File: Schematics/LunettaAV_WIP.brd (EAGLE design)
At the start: 52 parts, among them IC1 TLC339P, IC2 7805T, IC3 4046N, IC4 4040N, IC5 4017N, IC6 4051N, IC7 4094N, IC8 4046N, IC9 40106N, U1 LM358

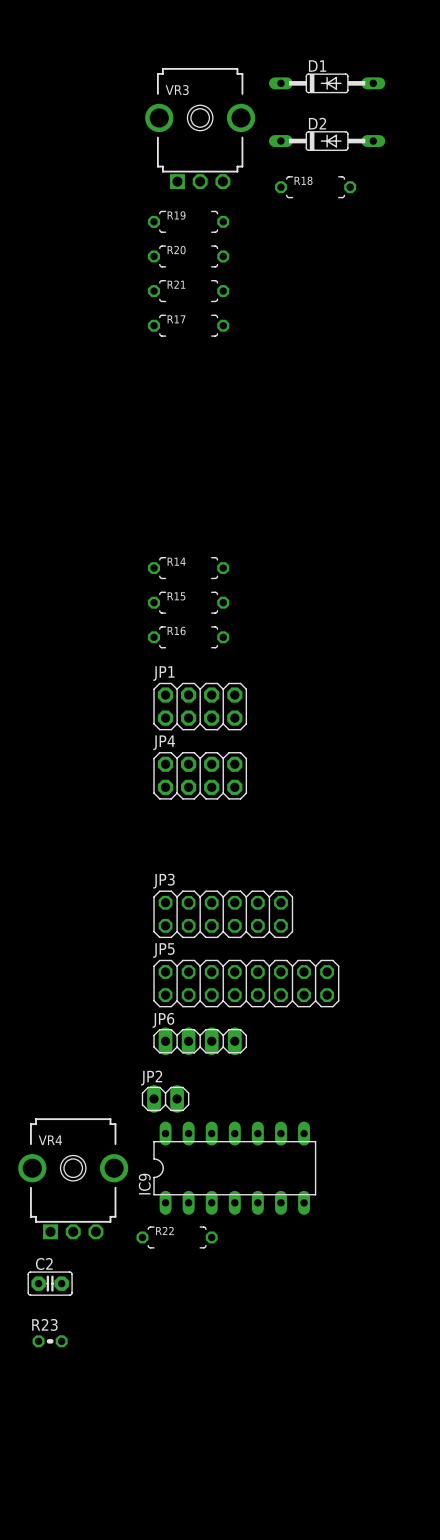
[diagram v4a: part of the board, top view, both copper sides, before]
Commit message: change melody out config and buffer the out for later stage
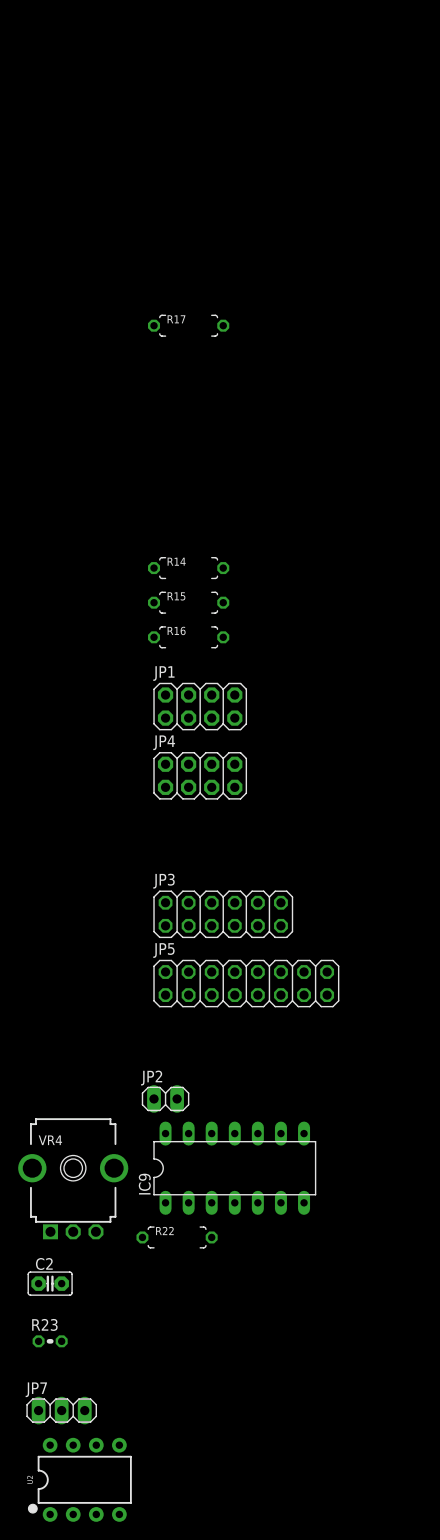
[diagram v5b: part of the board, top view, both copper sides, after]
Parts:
- removed D1, D2: 1N4148, diode:DO35-10
- removed JP6: (no value), pinhead:1X04
- removed R18, R19, R20: 100K, MusicThingModular:7MM_RESISTOR
- removed R21: 10K, MusicThingModular:7MM_RESISTOR
- removed VR3: 100K, MusicThingModular:9MM_SNAP-IN_POT
- added JP7: (no value), pinhead:1X03
- added U2: LM358, SparkFun-IC-Amplifiers:DIP08
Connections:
- removed net DRONEOUT: R20.1, VR3.2
- removed net GATEIN: JP6.4, R18.1
- removed net MIX: R19.2, R20.2, R21.2
- removed net N$7: D1.A, D2.A, R18.2
- removed net VCAOUT: D2.C, R19.1
- new net BUFFMEL: U2.6, U2.7
- net 9V: now also U2.8
- net GND: now also U2.4; no longer R21.1, VR3.1
- net MELODYOUT: now also U2.5; no longer D1.C, VR3.3
- net MOOX: now also JP7.3; no longer JP6.1
- net MOXO: now also JP7.2; no longer JP6.2
- net MXOO: now also JP7.1; no longer JP6.3

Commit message: PT2399 init + screen changed
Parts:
- removed DISP$1, DISP$2: DISPLAY-OLED-128X64-I2C, diy-modules:DISPLAY-OLED-128X64-I2C
- added C10, C8, C9: 10uF, SparkFun-Capacitors:CPOL-RADIAL-2.5MM-5MM
- added C11: 47uF, SparkFun-Capacitors:CPOL-RADIAL-2.5MM-5MM
- added C12, C13, C4, C5, C6, C7: 0.1uF, SparkFun-Capacitors:CAP-PTH-SMALL-KIT
- added C3: 100uF, SparkFun-Capacitors:CPOL-RADIAL-2.5MM-6.5MM
- added DD1: PT2399, ic-princeton-technologies:DIP-16
- added IC10: (no value), v-reg:78XXS
- added J1: POWER_JACKPOWER_JACK_SLOT, SparkFun-Connectors:POWER_JACK_PTH_SLOT
- added R13: (no value), MusicThingModular:7MM_RESISTOR
- added R18: 10k, MusicThingModular:7MM_RESISTOR
- added R19: 100k, MusicThingModular:7MM_RESISTOR
- added U$1, U$2: OLED_0.96_I2C, tft_1_8_1_44_oled_0_96:OLED_0.96_I2C
- added VR3: (no value), MusicThingModular:9MM_SNAP-IN_POT
- C1: value 1uF -> 10nF
- IC2: value 7805T -> 7805; device linear:TO220H -> v-reg:78XXS
- moved IC2 270.2 mm to (-138.4, -189.2)
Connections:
- new net DCIN: C10.1, IC10.IN, J1.PWR
- new net N$12: C6.1, DD1.10
- new net N$13: C7.2, DD1.11
- new net N$14: C7.1, DD1.12
- new net N$15: DD1.6, R13.2
- new net N$16: C11.1, DD1.2
- new net N$17: C5.2, DD1.7
- new net N$18: C4.1, DD1.8
- new net N$29: DD1.16, R18.1, R19.2
- new net N$30: DD1.15, R18.2
- new net N$7: C6.2, DD1.9
- net 3V3: now also C12.1, C13.1, U$1.VCC, U$2.VCC; no longer DISP$1.2, DISP$2.2
- net 5V: now also C3.1, C9.1, DD1.1, IC2.OUT; no longer IC2.3
- net 9V: now also C8.1, IC10.OUT, IC2.IN; no longer IC2.1
- net BUFFMEL: now also R19.1
- net GND: now also C10.2, C11.2, C12.2, C13.2, C3.2, C4.2, C5.1, C8.2, C9.2, DD1.3, DD1.4, IC10.GND, IC2.GND, J1.GND, U$1.GND, U$2.GND; no longer DISP$1.1, DISP$2.1, IC2.2
- net N$3: now also U$1.SCL, U$2.SCL; no longer DISP$1.3, DISP$2.3
- net N$4: now also U$1.SDA, U$2.SDA; no longer DISP$1.4, DISP$2.4
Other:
- board outline added: 7 x 7 mm

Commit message: PT Delay and other fixes
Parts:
- removed JP7: (no value), pinhead:1X03
- removed U$1, U$2: OLED_0.96_I2C, tft_1_8_1_44_oled_0_96:OLED_0.96_I2C
- added C14: .1uF, capacitor-wima:C2.5-2
- added C15, C16, C17, C19, C20, C21, C22: 0.1uF, SparkFun-Capacitors:CAP-PTH-SMALL-KIT
- added C18: 47uF, SparkFun-Capacitors:CPOL-RADIAL-2.5MM-5MM
- added C23: 100uF, SparkFun-Capacitors:CPOL-RADIAL-2.5MM-6.5MM
- added CLOCK-OUT, J3: WQP-PJ301M-12_JACK, MusicThingModular:WQP-PJ301M-12_JACK
- added D1: BAT42, diode:DO35-10
- added J2: (no value), SparkFun-Connectors:1X04_LONGPADS
- added OL96$1, OL96$2: OLED_0.96_I2C, tft_1_8_1_44_oled_0_96:OLED_0.96_I2C
- added R20: 10K, MusicThingModular:7MM_RESISTOR
- added R21: (no value), MusicThingModular:7MM_RESISTOR
- added VR5: (no value), MusicThingModular:9MM_SNAP-IN_POT
- C1: value 10nF -> 0.1uF; device SparkFun-Capacitors:CAP-PTH-10MM -> SparkFun-Capacitors:CAP-PTH-SMALL-KIT
- C10: value 10uF -> 10nF; device SparkFun-Capacitors:CPOL-RADIAL-2.5MM-5MM -> SparkFun-Capacitors:CAP-PTH-10MM
- C11: value 47uF -> 0.1uF; device SparkFun-Capacitors:CPOL-RADIAL-2.5MM-5MM -> SparkFun-Capacitors:CAP-PTH-SMALL-KIT
- C2: value .1uF -> 10uF; device capacitor-wima:C2.5-2 -> SparkFun-Capacitors:CPOL-RADIAL-2.5MM-5MM
- C3: value 100uF -> 10uF; device SparkFun-Capacitors:CPOL-RADIAL-2.5MM-6.5MM -> SparkFun-Capacitors:CPOL-RADIAL-2.5MM-5MM
- C5: value 0.1uF -> 10uF; device SparkFun-Capacitors:CAP-PTH-SMALL-KIT -> SparkFun-Capacitors:CPOL-RADIAL-2.5MM-5MM
- C8, C9: value 10uF -> 0.1uF; device SparkFun-Capacitors:CPOL-RADIAL-2.5MM-5MM -> SparkFun-Capacitors:CAP-PTH-SMALL-KIT
- IC1: value TLC339P -> 7809\; device linear:DIL14 -> v-reg:78XXS
- IC10: value (none) -> 4051N; device v-reg:78XXS -> 40xx:DIL16
- IC3: value 4046N -> 4040N
- IC4: value 4040N -> TLC339P; device 40xx:DIL16 -> linear:DIL14
- IC5: value 4017N -> 4046N
- IC6: value 4051N -> 4094N
- IC7: value 4094N -> 40106N; device 40xx:DIL16 -> 40xx:DIL14
- IC9: value 40106N -> 4017N; device 40xx:DIL14 -> 40xx:DIL16
- JP1: device adafruit:2X04 -> pinhead:1X02
- JP2: device pinhead:1X02 -> adafruit:2X04
- JP4: device adafruit:2X04 -> pinhead:2X08
- JP5: device pinhead:2X08 -> pinhead:1X03
- R1, R2: value 10K -> 4.7K; device MusicThingModular:7MM_RESISTOR -> MusicThingModular:10MM_RESISTOR
- R13: value (none) -> 1K
- R14: value 10K -> 1K
- R15: value 10K -> LDR; device MusicThingModular:7MM_RESISTOR -> rcl:0204V
- R16: value 10K -> 100k
- R17: value 1K -> 10k
- R18: value 10k -> 10K
- R19: value 100k -> 10K
- R22: value 1K -> (none)
- R23: value LDR -> (none); device rcl:0204V -> MusicThingModular:7MM_RESISTOR
- R3: value 10K -> 1K; device MusicThingModular:7MM_RESISTOR -> MusicThingModular:10MM_RESISTOR
- R5: value 1K -> 10K; device MusicThingModular:10MM_RESISTOR -> MusicThingModular:7MM_RESISTOR
- R6, R9: value 4.7K -> 10K; device MusicThingModular:10MM_RESISTOR -> MusicThingModular:7MM_RESISTOR
- S1, S2, S3: value (none) -> MOMENTARY-SWITCH-SPST-PTH-12MM
- VR3: value (none) -> 100K
- VR4: value 100K -> (none)
- moved R19 415.3 mm to (-78.7, 114.3)
- moved C13 415.0 mm to (-67.3, 118.1)
- moved R18 414.3 mm to (-68.6, 114.3)
- moved C12 413.3 mm to (-61.0, 118.1)
- moved C11 409.7 mm to (-54.6, 118.1)
- moved C3 370.4 mm to (-102.9, 94.0)
- moved R13 355.2 mm to (-27.9, 114.3)
- moved C8 334.9 mm to (-41.9, 118.1)
- moved C9 334.9 mm to (-48.3, 118.1)
- moved C10 325.2 mm to (-71.1, 102.9)
- moved C7 322.5 mm to (-35.6, 118.1)
- moved C6 321.1 mm to (-29.2, 118.1)
- moved C4 316.3 mm to (-22.9, 118.1)
- moved J1 312.2 mm to (-43.2, 83.8)
- moved C5 309.4 mm to (-16.5, 104.1)
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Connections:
- removed net VDD: IC9.14
- removed net VSS: IC9.7
- new net N$31: C19.2, DD1.11
- new net N$32: CLOCK-OUT.P$1_TIP, D1.C
- new net OUT: VR5.2
- net 3V3: now also C1.1, C4.1, OL96$1.VCC, OL96$2.VCC, R1.2, R2.2, R5.2; no longer C12.1, C13.1, R10.2, R11.2, R9.2, U$1.VCC, U$2.VCC
- net 5V: now also C23.1, C5.1, IC4.10, IC4.4, IC4.6, IC4.8, JP1.1; no longer C3.1, C9.1, IC1.10, IC1.4, IC1.6, IC1.8, JP2.1
- net 9V: now also C11.1, C12.1, C13.1, C15.1, C16.1, C17.1, C3.1, C6.1, C7.1, C9.1, IC1.OUT, IC10.16, IC4.3, IC6.1, IC6.15, IC7.14, IC9.16, R13.1; no longer IC1.3, IC10.OUT, IC4.16, IC7.1, IC7.15, IC7.16, R22.1
- net ANALOGIN1: no longer U1.3
- net ANALOGIN2: now also U1.3
- net AUDIORATE: now also IC7.6, IC9.14; no longer IC5.14, IC9.6
- net BUFFCLOCK: now also IC6.3, R22.1; no longer IC7.3
- net BUFFMEL: now also R16.1, VR5.3; no longer R19.1
- net CLOCKSELECT: now also JP2.2, JP2.4, JP2.6, JP2.8; no longer JP4.2, JP4.4, JP4.6, JP4.8
- net DCIN: now also C2.1, IC1.IN; no longer C10.1, IC10.IN
- net DIN1: now also R3.2; no longer R5.2
- net GND: now also C1.2, C14.2, C15.2, C16.2, C17.2, C18.2, C19.1, C20.1, C22.2, C23.2, C5.2, C6.2, C7.2, CLOCK-OUT.P$3_SLEEVE, DD1.12, IC1.GND, IC10.6, IC10.7, IC10.8, IC4.12, IC5.5, IC7.11, IC7.13, IC7.7, IC7.9, IC9.8, OL96$1.GND, OL96$2.GND, R10.1, R11.1, R18.1, R19.1, R20.1, R23.2, R9.1, VR4.1, VR5.1; no longer C10.2, C5.1, IC1.12, IC10.GND, IC3.5, IC4.8, IC5.13, IC6.6, IC6.7, IC7.8, IC9.11, IC9.9, R1.1, R14.1, R15.1, R16.1, R2.1, R5.1, U$1.GND, U$2.GND
- net MELODYOUT: now also IC9.3; no longer IC5.3
- net MOOX: now also IC10.9, JP5.3, R20.2; no longer IC6.9, JP7.3, R16.2
- net MOXO: now also IC10.10, JP5.2, R19.2; no longer IC6.10, JP7.2, R15.2
- net MXOO: now also IC10.11, JP5.1, R18.2; no longer IC6.11, JP7.1, R14.2
- net N$1: now also JP1.2; no longer JP2.2
- net N$10: now also IC7.4, IC7.5; no longer IC9.4, IC9.5
- net N$11: now also C14.1, IC7.1, R15.2, VR3.2; no longer C2.1, IC9.1, R23.2, VR4.2
- net N$12: now also C21.1; no longer C6.1
- net N$13: now also R22.2, R23.1, U2.3; no longer C7.2, DD1.11
- net N$14: now also D1.A, U2.1, U2.2; no longer C7.1, DD1.12
- net N$15: now also R21.2; no longer R13.2
- net N$16: now also C18.1; no longer C11.1
- net N$17: now also C20.2; no longer C5.2
- net N$18: now also C22.1; no longer C4.1
- net N$19: now also IC10.3, IC9.15; no longer IC5.15, IC6.3
- net N$2: now also C10.2, IC5.7; no longer C1.2, IC3.7
- net N$20: now also IC10.13, IC9.4; no longer IC5.4, IC6.13
- net N$21: now also IC10.14, IC9.7; no longer IC5.7, IC6.14
- net N$22: now also IC10.15, IC9.10; no longer IC5.10, IC6.15
- net N$23: now also IC10.12, IC9.1; no longer IC5.1, IC6.12
- net N$24: now also IC10.1, IC9.5; no longer IC5.5, IC6.1
- net N$25: now also IC10.5, IC9.6; no longer IC5.6, IC6.5
- net N$26: now also IC10.2, IC9.9; no longer IC5.9, IC6.2
- net N$27: now also IC10.4, IC9.11; no longer IC5.11, IC6.4
- net N$28: now also IC6.2, R14.1; no longer IC7.2, R17.1
- net N$29: now also R16.2, R17.1; no longer R18.1, R19.2
- net N$3: now also OL96$1.SCL, OL96$2.SCL, R1.1; no longer R6.1, U$1.SCL, U$2.SCL
- net N$30: now also R17.2, VR4.2; no longer R18.2
- net N$4: now also OL96$1.SDA, OL96$2.SDA, R2.1; no longer R9.1, U$1.SDA, U$2.SDA
- net N$5: now also C10.1, IC5.6; no longer C1.1, IC3.6
- net N$6: now also IC5.11; no longer IC3.11
- net N$7: now also C21.2; no longer C6.2
- net N$8: now also R13.2; no longer R22.2
- net N$9: now also IC7.2, IC7.3, R15.1, VR3.3; no longer IC9.2, IC9.3, R23.1, VR4.3
- net OOX: now also IC4.11, J2.4, R11.2; no longer IC1.11, JP1.1, JP1.2, R8.2
- net OXO: now also IC4.9, J2.3, R10.2; no longer IC1.9, JP1.3, JP1.4, R3.2
- net PLL/16: now also IC3.5; no longer IC4.5
- net PLL/2: now also IC3.9, JP2.3; no longer IC4.9, JP4.3
- net PLL/32: now also IC3.3; no longer IC4.3
- net PLL/4: now also IC3.7, JP2.5; no longer IC4.7, JP4.5
- net PLL/8: now also IC3.6, JP2.7; no longer IC4.6, JP4.7
- net PLLCLOCKOUT: now also IC3.10, IC5.4, JP2.1; no longer IC3.4, IC4.10, JP4.1
- net RESET: now also IC4.5, J2.1, R8.2; no longer IC1.5, JP1.7, JP1.8, R1.2
- net SPEEDYBUFF: now also IC5.9; no longer IC3.9
- net SR1: now also IC6.4, JP4.1, JP4.2; no longer IC7.4, JP5.1, JP5.2
- net SR2: now also IC6.5, JP4.3, JP4.4; no longer IC7.5, JP5.3, JP5.4
- net SR3: now also IC6.6, JP4.5, JP4.6; no longer IC7.6, JP5.5, JP5.6
- net SR4: now also IC6.7, JP4.7, JP4.8; no longer IC7.7, JP5.7, JP5.8
- net SR5: now also IC6.14, JP4.10, JP4.9; no longer IC7.14, JP5.10, JP5.9
- net SR6: now also IC6.13, JP4.11, JP4.12; no longer IC7.13, JP5.11, JP5.12
- net SR7: now also IC6.12, JP4.13, JP4.14; no longer IC7.12, JP5.13, JP5.14
- net SR8: now also IC6.11, JP4.15, JP4.16, R14.2; no longer IC7.11, JP5.15, JP5.16, R17.2
- net TNSYOOX: now also IC4.13, R7.1; no longer IC1.13, R11.1
- net TNSYOXO: now also IC4.14, R6.1; no longer IC1.14, R10.1
- net TNSYRES: now also IC4.2; no longer IC1.2
- net TNSYXOO: now also IC4.1, R5.1; no longer IC1.1, R7.1
- net XOO: now also IC4.7, J2.2, R9.2; no longer IC1.7, JP1.5, JP1.6, R2.2
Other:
- board size 7 x 7 mm -> 160 x 100 mm

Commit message: update schematics to match new code
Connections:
- net DIN1: now also B1.9; no longer B1.12
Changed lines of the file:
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@@
 </signal>
 <signal name="DIN1">
-<contactref element="B1" pad="12"/>
 <contactref element="R3" pad="2"/>
 <contactref element="S1" pad="3"/>
-<wire x1="-15.24" y1="36.83" x2="-13.97" y2="110.49" width="0" layer="19" extent="1-1"/>
-<wire x1="-90.27" y1="10.12" x2="-15.24" y2="36.83" width="0" layer="19" extent="1-1"/>
+<contactref element="B1" pad="9"/>
+<wire x1="-15.24" y1="29.21" x2="-13.97" y2="110.49" width="0" layer="19" extent="1-1"/>
+<wire x1="-90.27" y1="10.12" x2="-15.24" y2="29.21" width="0" layer="19" extent="1-1"/>
 </signal>
 <signal name="5V">
